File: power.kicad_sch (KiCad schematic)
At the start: 61 parts, among them J3 Conn_02x05_Odd_Even, T1 net-tie, U1 LMR54410, U2 RT9080-33GJ5, U3 TPS546D24ARVFR, U4 MIC5504

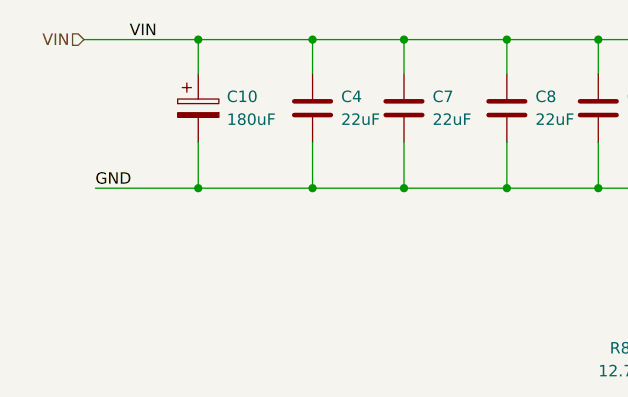
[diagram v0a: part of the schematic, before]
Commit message: Add tvs to 303
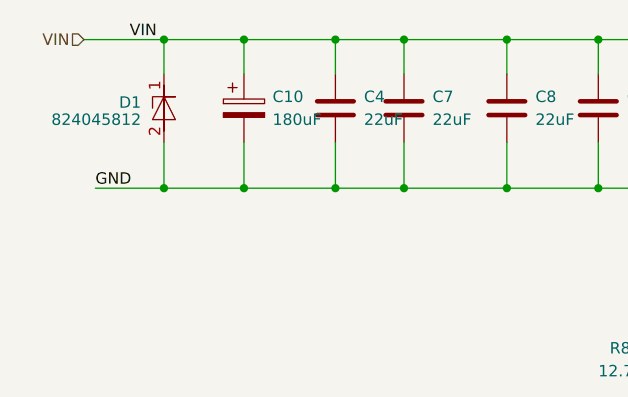
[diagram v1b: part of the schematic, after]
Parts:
- added D1: 824045812, bitaxe:824045812, symbol bitaxe:824045812
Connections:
- net GND: now also D1.2 (GND)
- net VIN: now also D1.1 (I/O)
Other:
- moved on the sheet: C10, C4
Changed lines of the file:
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@@
 	)
 	(junction
+		(at 49.53 36.83)
+		(diameter 0)
+		(color 0 0 0 0)
+	)
+	(junction
 		(at 33.02 172.72)
 		(diameter 0)
@@
 	)
 	(junction
-		(at 34.29 36.83)
-		(diameter 0)
-		(color 0 0 0 0)
-	)
-	(junction
 		(at 124.46 45.72)
 		(diameter 0)
@@
 	)
 	(junction
-		(at 46.99 36.83)
-		(diameter 0)
-		(color 0 0 0 0)
-	)
-	(junction
 		(at 57.15 20.32)
 		(diameter 0)
@@
 	)
 	(junction
+		(at 30.48 20.32)
+		(diameter 0)
+		(color 0 0 0 0)
+	)
+	(junction
 		(at 110.49 20.32)
 		(diameter 0)
@@
 	)
 	(junction
+		(at 49.53 20.32)
+		(diameter 0)
+		(color 0 0 0 0)
+	)
+	(junction
 		(at 162.56 73.66)
 		(diameter 0)
@@
 	)
 	(junction
-		(at 46.99 20.32)
+		(at 39.37 20.32)
 		(diameter 0)
 		(color 0 0 0 0)
@@
 	)
 	(junction
-		(at 34.29 20.32)
+		(at 30.48 36.83)
 		(diameter 0)
 		(color 0 0 0 0)
@@
 	)
 	(junction
+		(at 39.37 36.83)
+		(diameter 0)
+		(color 0 0 0 0)
+	)
+	(junction
 		(at 194.31 93.98)
 		(diameter 0)
@@
 	(wire
 		(pts
+			(xy 30.48 36.83) (xy 39.37 36.83)
+		)
+		(stroke
+			(width 0)
+			(type default)
+		)
+	)
+	(wire
+		(pts
 			(xy 203.2 146.05) (xy 208.28 146.05)
 		)
@@
 	(wire
 		(pts
-			(xy 57.15 20.32) (xy 46.99 20.32)
+			(xy 57.15 20.32) (xy 49.53 20.32)
 		)
 		(stroke
@@
 	(wire
 		(pts
-			(xy 46.99 31.75) (xy 46.99 36.83)
+			(xy 49.53 31.75) (xy 49.53 36.83)
 		)
 		(stroke
@@
 	(wire
 		(pts
-			(xy 46.99 20.32) (xy 34.29 20.32)
+			(xy 39.37 20.32) (xy 49.53 20.32)
 		)
 		(stroke
@@
 	(wire
 		(pts
-			(xy 22.86 36.83) (xy 34.29 36.83)
+			(xy 22.86 36.83) (xy 30.48 36.83)
 		)
 		(stroke
@@
 	(wire
 		(pts
-			(xy 46.99 36.83) (xy 57.15 36.83)
+			(xy 90.17 36.83) (xy 101.6 36.83)
 		)
 		(stroke
@@
 	(wire
 		(pts
-			(xy 90.17 36.83) (xy 101.6 36.83)
+			(xy 30.48 20.32) (xy 30.48 24.13)
 		)
 		(stroke
@@
 	(wire
 		(pts
-			(xy 48.26 119.38) (xy 175.26 119.38)
+			(xy 30.48 31.75) (xy 30.48 36.83)
 		)
 		(stroke
@@
 	(wire
 		(pts
-			(xy 135.89 139.7) (xy 135.89 146.05)
+			(xy 48.26 119.38) (xy 175.26 119.38)
 		)
 		(stroke
@@
 	(wire
 		(pts
-			(xy 162.56 76.2) (xy 158.75 76.2)
+			(xy 135.89 139.7) (xy 135.89 146.05)
 		)
 		(stroke
@@
 	(wire
 		(pts
-			(xy 64.77 184.15) (xy 60.96 184.15)
+			(xy 162.56 76.2) (xy 158.75 76.2)
 		)
 		(stroke
@@
 	(wire
 		(pts
-			(xy 248.92 93.98) (xy 254 93.98)
+			(xy 64.77 184.15) (xy 60.96 184.15)
 		)
 		(stroke
@@
 	(wire
 		(pts
-			(xy 34.29 36.83) (xy 46.99 36.83)
+			(xy 248.92 93.98) (xy 254 93.98)
 		)
 		(stroke
@@
 	(wire
 		(pts
+			(xy 30.48 20.32) (xy 39.37 20.32)
+		)
+		(stroke
+			(width 0)
+			(type default)
+		)
+	)
+	(wire
+		(pts
 			(xy 48.26 82.55) (xy 130.81 82.55)
 		)
@@
 	(wire
 		(pts
-			(xy 34.29 31.75) (xy 34.29 36.83)
+			(xy 39.37 31.75) (xy 39.37 36.83)
 		)
 		(stroke
@@
 	(wire
 		(pts
-			(xy 46.99 20.32) (xy 46.99 24.13)
+			(xy 49.53 20.32) (xy 49.53 24.13)
 		)
 		(stroke
@@
 	(wire
 		(pts
-			(xy 34.29 24.13) (xy 34.29 20.32)
+			(xy 39.37 24.13) (xy 39.37 20.32)
 		)
 		(stroke
@@
 	(wire
 		(pts
-			(xy 21.59 20.32) (xy 34.29 20.32)
+			(xy 21.59 20.32) (xy 30.48 20.32)
 		)
 		(stroke
@@
 	(wire
 		(pts
+			(xy 39.37 36.83) (xy 49.53 36.83)
+		)
+		(stroke
+			(width 0)
+			(type default)
+		)
+	)
+	(wire
+		(pts
 			(xy 162.56 49.53) (xy 162.56 46.99)
 		)
@@
 	(wire
 		(pts
+			(xy 49.53 36.83) (xy 57.15 36.83)
+		)
+		(stroke
+			(width 0)
+			(type default)
+		)
+	)
+	(wire
+		(pts
 			(xy 101.6 146.05) (xy 104.14 146.05)
 		)
@@
 	(symbol
 		(lib_id "Device:C")
-		(at 46.99 27.94 0)
+		(at 49.53 27.94 0)
 		(unit 1)
 		(exclude_from_sim no)
@@
 		(fields_autoplaced yes)
 		(property "Reference" "C4"
-			(at 50.165 26.67 0)
+			(at 52.705 26.67 0)
 			(effects
 				(font
@@
 		)
 		(property "Value" "22uF"
-			(at 50.165 29.21 0)
+			(at 52.705 29.21 0)
 			(effects
 				(font
@@
 		)
 		(property "Footprint" "Capacitor_SMD:C_1210_3225Metric"
-			(at 47.9552 31.75 0)
+			(at 50.4952 31.75 0)
 			(effects
 				(font
@@
 		)
 		(property "Datasheet" "~"
-			(at 46.99 27.94 0)
+			(at 49.53 27.94 0)
 			(effects
 				(font
@@
 		)
 		(property "Description" ""
-			(at 46.99 27.94 0)
+			(at 49.53 27.94 0)
 			(effects
 				(font
@@
 		)
 		(property "DK" "490-3889-1-ND"
-			(at 46.99 27.94 0)
+			(at 49.53 27.94 0)
 			(effects
 				(font
@@
 		)
 		(property "PARTNO" "GRM32ER61E226KE15L"
-			(at 46.99 27.94 0)
+			(at 49.53 27.94 0)
 			(effects
 				(font
@@
 	)
 	(symbol
+		(lib_id "bitaxe:824045812")
+		(at 30.48 27.94 90)
+		(mirror x)
+		(unit 1)
+		(exclude_from_sim no)
+		(in_bom yes)
+		(on_board yes)
+		(dnp no)
+		(property "Reference" "D1"
+			(at 27.94 27.3049 90)
+			(effects
+				(font
+					(size 1.27 1.27)
+				)
+				(justify left)
+			)
+		)
+		(property "Value" "824045812"
+			(at 27.94 29.21 90)
+			(effects
+				(font
+					(size 1.27 1.27)
+				)
+				(justify left)
+			)
+		)
+		(property "Footprint" "bitaxe:824045812"
+			(at 30.48 27.94 0)
+			(effects
+				(font
+					(size 1.27 1.27)
+				)
+				(hide yes)
+			)
+		)
+		(property "Datasheet" ""
+			(at 30.48 27.94 0)
+			(effects
+				(font
+					(size 1.27 1.27)
+				)
+				(hide yes)
+			)
+		)
+		(property "Description" ""
+			(at 30.48 27.94 0)
+			(effects
+				(font
+					(size 1.27 1.27)
+				)
+				(hide yes)
+			)
+		)
+		(property "JLC" "824045812"
+			(at 30.48 27.94 90)
+			(effects
+				(font
+					(size 1.27 1.27)
+				)
+				(hide yes)
+			)
+		)
+		(pin "1"
+		)
+		(pin "2"
+		)
+		(instances
+			(project "bitaxeHex"
+				(path "/e63e39d7-6ac0-4ffd-8aa3-1841a4541b55/8ec0a9c6-2b78-44ef-a83d-9047d2828409"
+					(reference "D1")
+					(unit 1)
+				)
+			)
+		)
+	)
+	(symbol
 		(lib_id "Device:R_US")
 		(at 203.2 109.22 180)
@@
 	(symbol
 		(lib_id "Device:C_Polarized")
-		(at 34.29 27.94 0)
+		(at 39.37 27.94 0)
 		(unit 1)
 		(exclude_from_sim no)
@@
 		(dnp no)
 		(property "Reference" "C10"
-			(at 37.465 26.67 0)
+			(at 42.545 26.67 0)
 			(effects
 				(font
@@
 		)
 		(property "Value" "180uF"
-			(at 37.465 29.21 0)
+			(at 42.545 29.21 0)
 			(effects
 				(font
@@
 		)
 		(property "Footprint" "Capacitor_SMD:CP_Elec_6.3x5.9"
-			(at 35.2552 31.75 0)
+			(at 40.3352 31.75 0)
 			(effects
 				(font
@@
 		)
 		(property "Datasheet" "https://industrial.panasonic.com/cdbs/www-data/pdf/AAB8000/AAB8000C177.pdf"
-			(at 34.29 27.94 0)
+			(at 39.37 27.94 0)
 			(effects
 				(font
@@
 		)
 		(property "Description" ""
-			(at 34.29 27.94 0)
+			(at 39.37 27.94 0)
 			(effects
 				(font
@@
 		)
 		(property "DK" "P16479CT-ND"
-			(at 34.29 27.94 0)
+			(at 39.37 27.94 0)
 			(effects
 				(font
@@
 		)
 		(property "PARTNO" "16SVPF180M"
-			(at 34.29 27.94 0)
+			(at 39.37 27.94 0)
 			(effects
 				(font
@@
 		)
 		(property "HEIGHT" "5.9mm"
-			(at 34.29 27.94 0)
+			(at 39.37 27.94 0)
 			(effects
 				(font
